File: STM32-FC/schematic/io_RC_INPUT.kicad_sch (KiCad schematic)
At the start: 9 parts, among them J6 PWM_Conn_3x14, J7 ZH 1.5mm 3P, J8 ZH 1.5mm 4P, Q2 S9013

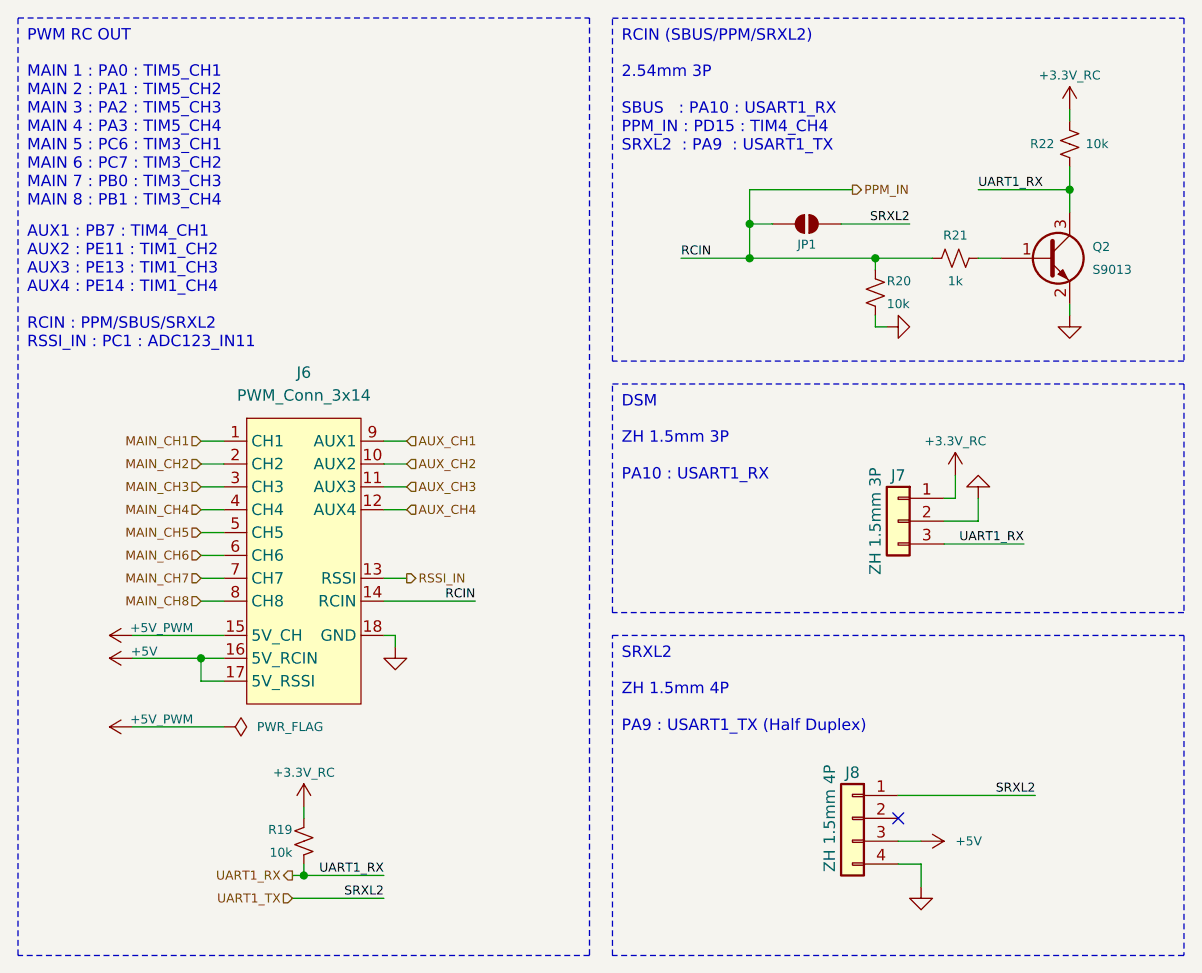
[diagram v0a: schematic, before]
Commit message: v1.0.1 update WIP
repactor and USB C bug fix
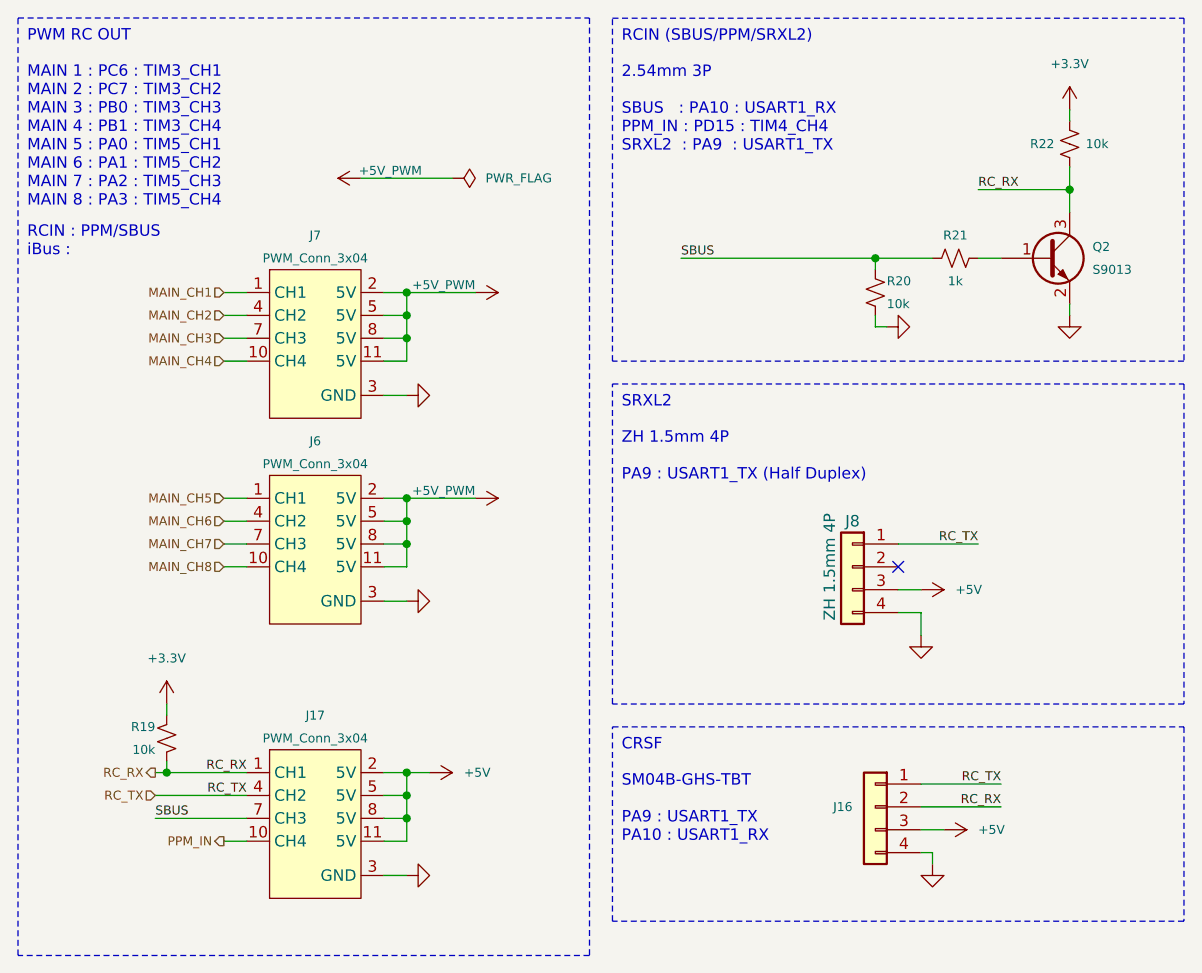
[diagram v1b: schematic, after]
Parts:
- removed J6: PWM_Conn_3x14, PWM_Connector:PWM_Conn_3x14, symbol PWM_Connector:PWM_Conn_3x14
- removed J7: ZH 1.5mm 3P, JST_ZH:JST_ZH_S3B-ZR-SM4A-TF_1x03-1MP_P1.50mm_Horizontal, symbol Connector_Generic:Conn_01x03
- removed JP1: SolderJumper_2_Open, Jumper:SolderJumper-2_P1.3mm_Open_TrianglePad1.0x1.5mm, symbol Jumper:SolderJumper_2_Open
- added J16: BM04B-GHS-TBT, Connector_JST:JST_GH_BM04B-GHS-TBT_1x04-1MP_P1.25mm_Vertical, symbol Connector_Generic:Conn_01x04
- added J17, J6, J7: PWM_Conn_3x04, PWM_Connector:PWM_Conn_3x04, symbol PWM_Connector:PWM_Conn_3x04_JLC
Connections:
- net +5V: now also J16.3 (Pin_3), J17.11 (5V), J17.2 (5V), J17.5 (5V), J17.8 (5V)
- net +5V_PWM: now also J6.11 (5V), J6.2 (5V), J6.5 (5V), J6.8 (5V), J7.11 (5V), J7.2 (5V), J7.5 (5V), J7.8 (5V)
- net GND: now also J16.4 (Pin_4), J17.12 (GND), J17.3 (GND), J17.6 (GND), J17.9 (GND), J6.12 (GND), J6.3 (GND), J6.6 (GND), J6.9 (GND), J7.12 (GND), J7.3 (GND), J7.6 (GND), J7.9 (GND)
- net MAIN_CH1: now also J7.1 (CH1)
- net MAIN_CH2: now also J7.4 (CH2)
- net MAIN_CH3: now also J7.7 (CH3)
- net MAIN_CH4: now also J7.10 (CH4)
- net MAIN_CH5: now also J6.1 (CH1)
- net MAIN_CH6: now also J6.4 (CH2)
- net MAIN_CH7: now also J6.7 (CH3)
- net MAIN_CH8: now also J6.10 (CH4)
- net PPM_IN: now also J17.10 (CH4); no longer R20.1, R21.1
- net +3.3V_RC renamed +3.3V
- net UART1_RX renamed RC_RX
- net RC_RX: now also J16.2 (Pin_2), J17.1 (CH1)
- net UART1_TX renamed RC_TX
- net RC_TX: now also J16.1 (Pin_1), J17.4 (CH2)
- new net SBUS: J17.7 (CH3), R20.1, R21.1
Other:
- note added: "CRSF"
- note added: "MAIN 1 : PC6 : TIM3_CH1 MAIN 2 : PC7 : TIM3_CH2 MAIN 3 : PB0 : TIM3_CH3 MAIN 4 : PB1 : TIM3_CH4 MAIN 5 : PA0 : TIM5_CH1 MAIN 6 : PA1 : TIM5_CH2 MAIN 7 : PA2 : TIM5_CH3 MAIN 8 : PA3 : TIM5_CH4"
- note added: "RCIN : PPM/SBUS iBus :"
- note added: "SM04B-GHS-TBT PA9 : USART1_TX PA10 : USART1_RX"
- note removed: "AUX1 : PB7 : TIM4_CH1 AUX2 : PE11 : TIM1_CH2 AUX3 : PE13 : TIM1_CH3 AUX4 : PE14 : TIM1_CH4 RCIN : PPM/SBUS/SRXL2 RSSI_IN : PC1 : ADC123_IN11"
- note removed: "DSM"
- note removed: "MAIN 1 : PA0 : TIM5_CH1 MAIN 2 : PA1 : TIM5_CH2 MAIN 3 : PA2 : TIM5_CH3 MAIN 4 : PA3 : TIM5_CH4 MAIN 5 : PC6 : TIM3_CH1 MAIN 6 : PC7 : TIM3_CH2 MAIN 7 : PB0 : TIM3_CH3 MAIN 8 : PB1 : TIM3_CH4"
- note removed: "ZH 1.5mm 3P PA10 : USART1_RX"
- moved on the sheet: J8, R19

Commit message: schematic update & lib update
- ICM-45686
- ICP-20100
- Micro SD update SDIO instead of SPI
- servo main output
- DC2DC buck instead power regulator
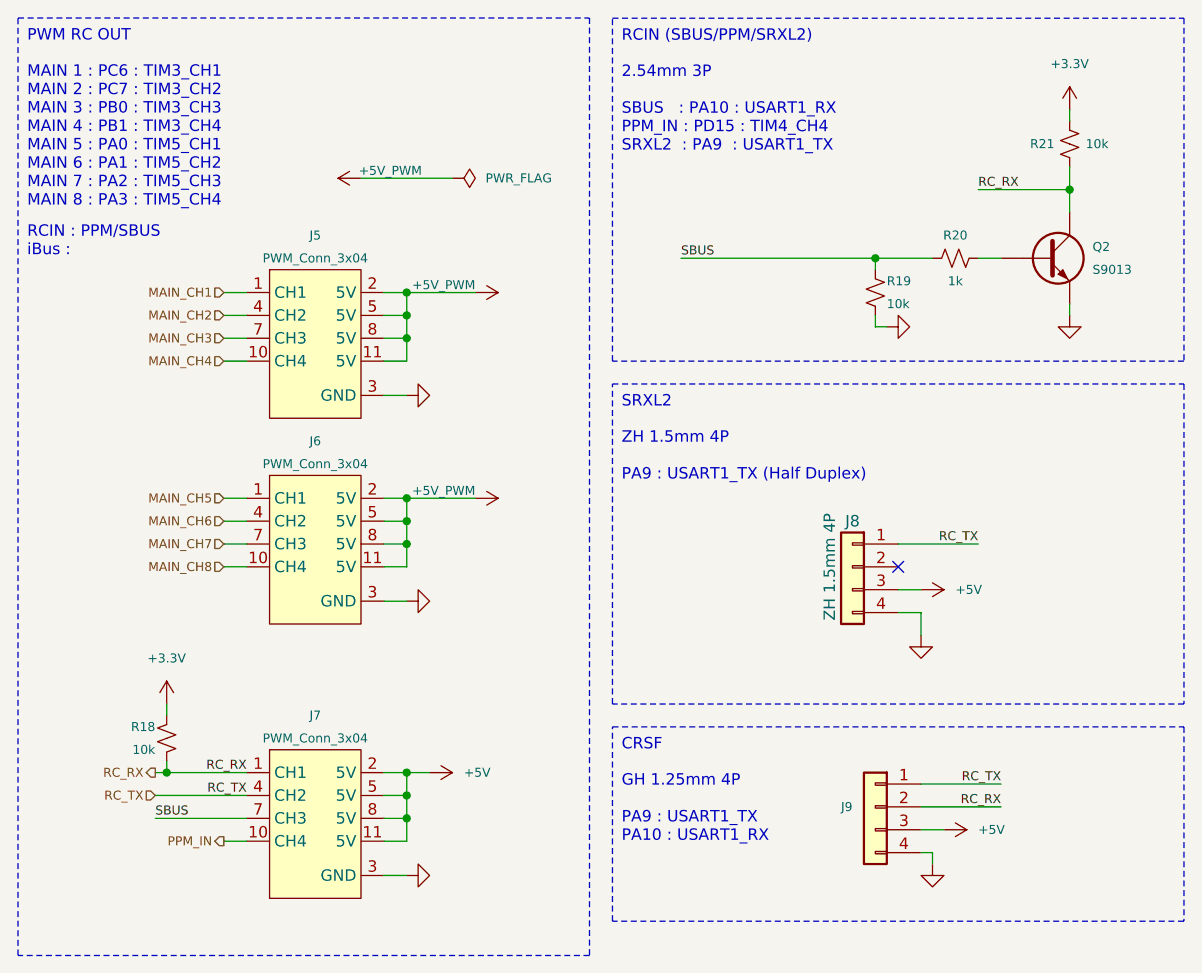
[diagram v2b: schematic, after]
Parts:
- J8: footprint JST_ZH:JST_ZH_S4B-ZR-SM4A-TF_1x04-1MP_P1.50mm_Horizontal -> Connector_JST:JST_ZH_B4B-ZR-SM4-TF_1x04-1MP_P1.50mm_Vertical
- J9: renamed from J16; value BM04B-GHS-TBT -> GH 1.25mm 4P
- Q2: symbol Device:Q_NPN_BEC -> Device:Q_NPN
- renumbered J7 to J5, J17 to J7, R19 to R18, R20 to R19, R21 to R20, R22 to R21
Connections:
- net GND: now also Q2.E; no longer Q2.2 (E)
- net RC_RX: now also Q2.C; no longer Q2.3 (C)
- net at R20.2: now also Q2.B; no longer Q2.1 (B)
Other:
- note added: "GH 1.25mm 4P PA9 : USART1_TX PA10 : USART1_RX"
- note removed: "SM04B-GHS-TBT PA9 : USART1_TX PA10 : USART1_RX"
- title: STM32 Flight Controller -> NARAEON - Flight Controller
